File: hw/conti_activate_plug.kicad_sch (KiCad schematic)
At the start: 38 parts, among them J1 Conn_01x02_Pin, J2 Conn_01x02_Pin, J3 Conn_01x02_Pin, J4 Conn_01x02_Pin, J5 Conn_01x02_Pin, J6 Conn_01x02_Pin, J7 Conn_01x02_Socket, Q1 BSS138, Q2 MMBTA06, Q3 BSS138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

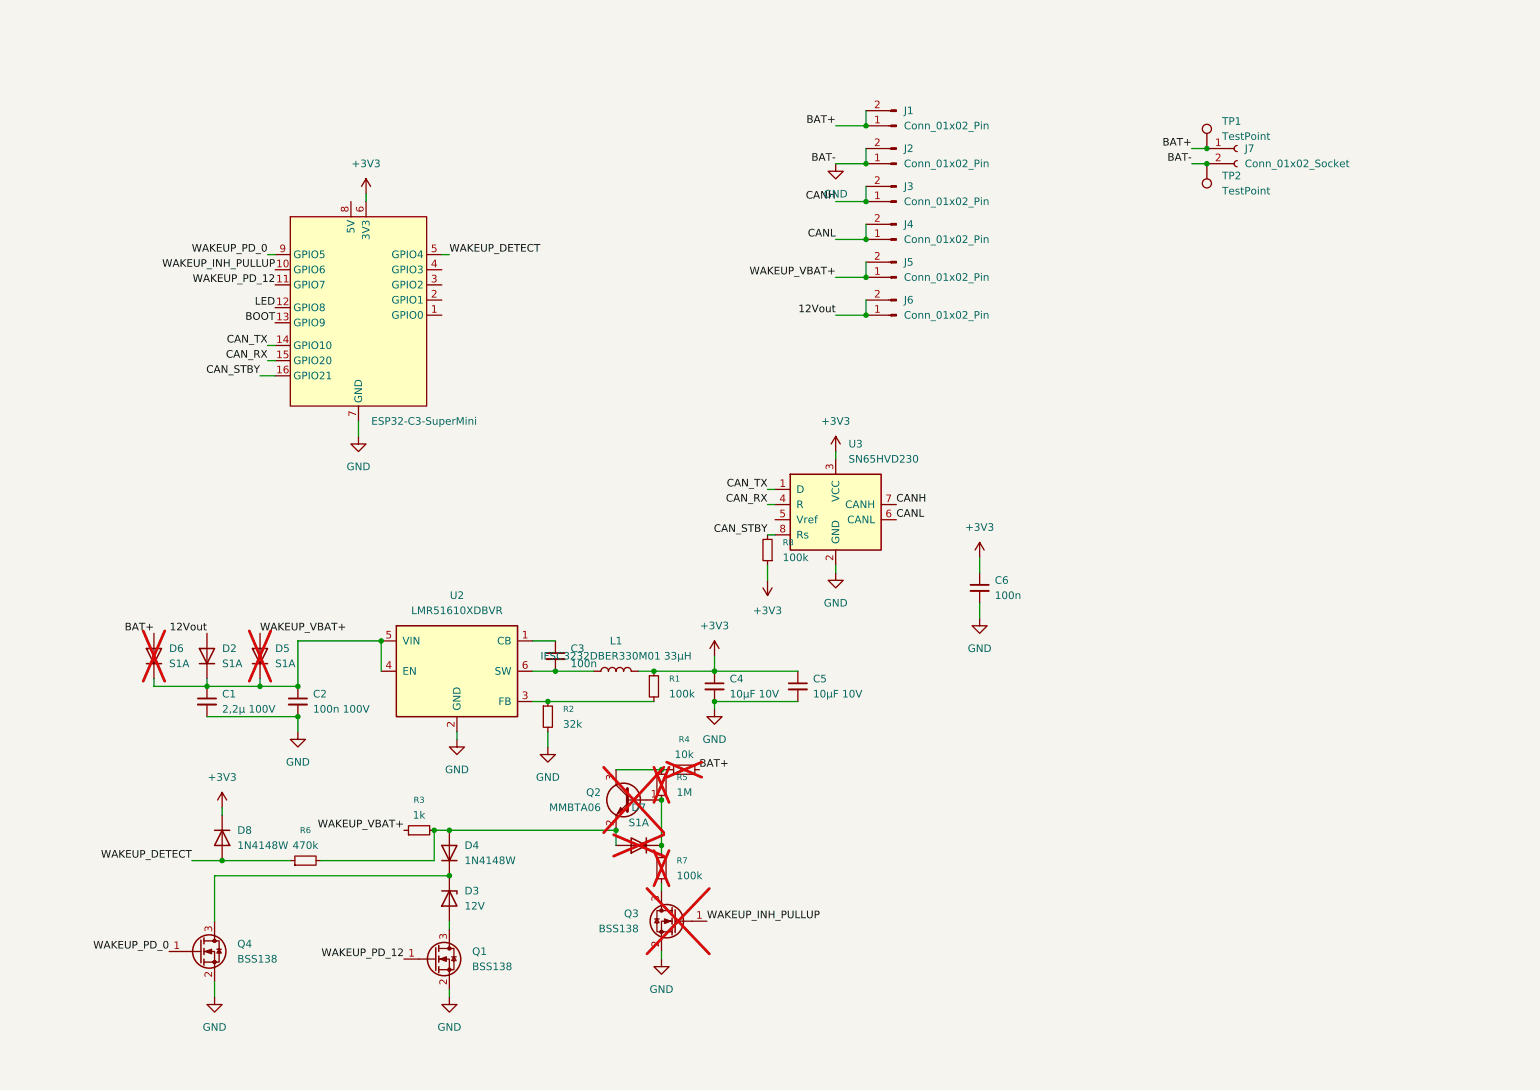
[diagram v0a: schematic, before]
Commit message: Vext, CAN Terminierung, Mounting-Hole
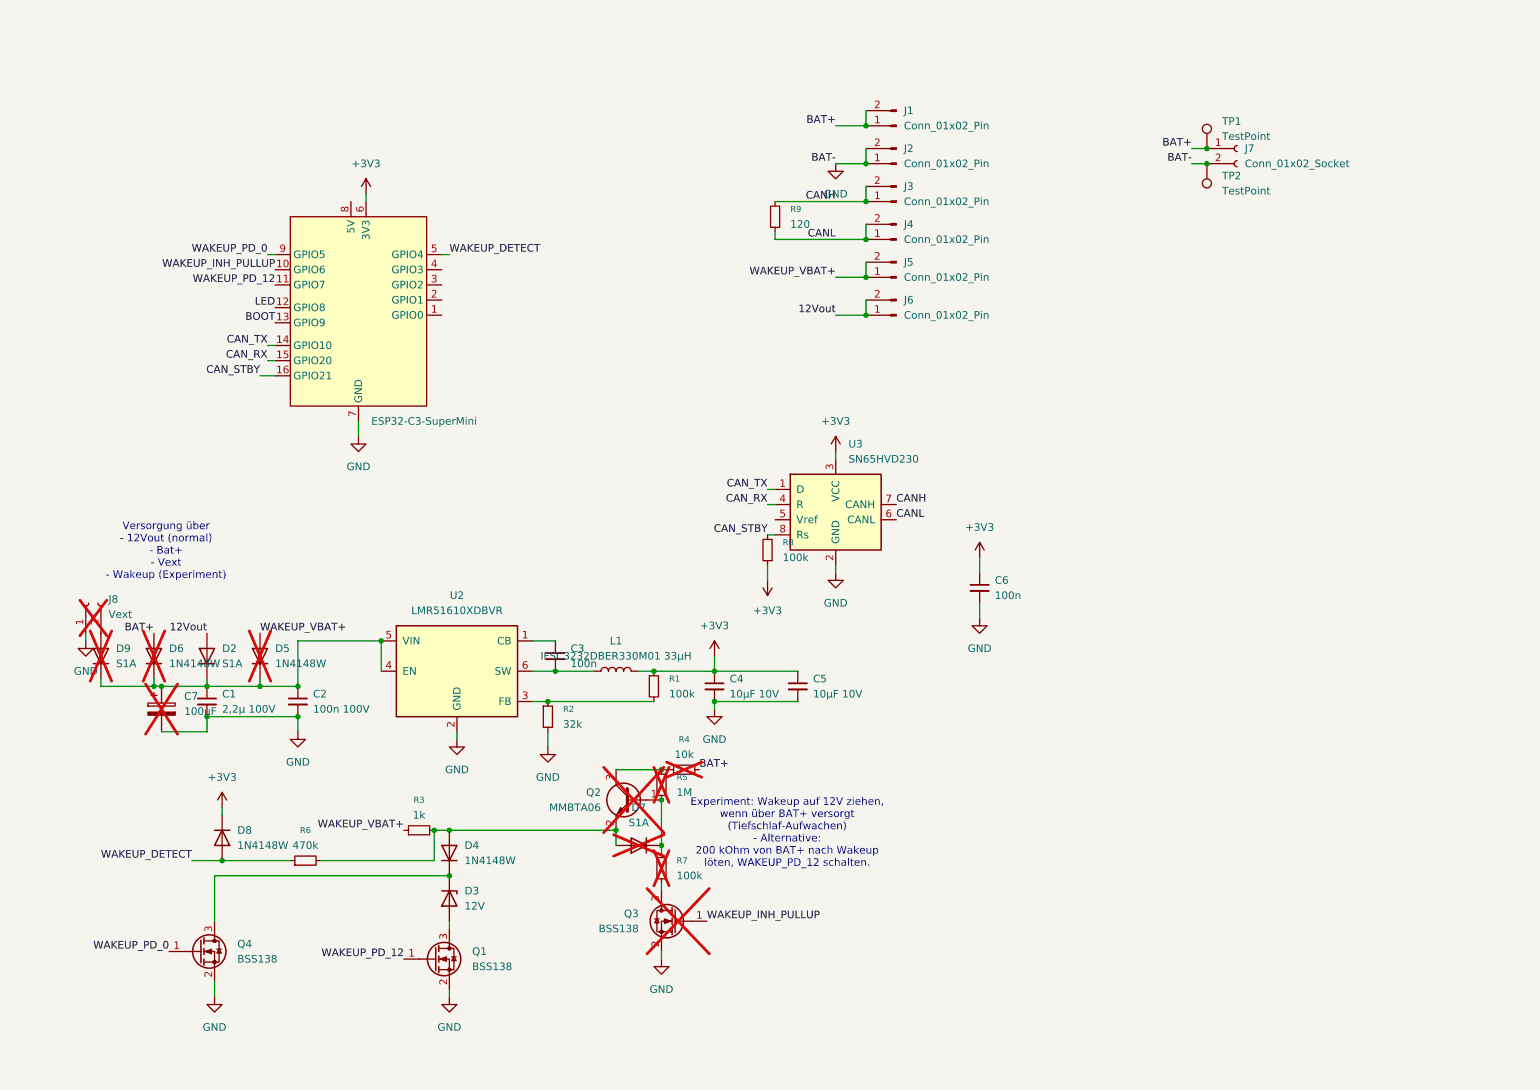
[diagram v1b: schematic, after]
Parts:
- added C7: 100µF, Capacitor_THT:CP_Radial_Tantal_D8.0mm_P5.00mm, symbol Device:C_Polarized
- added D9: S1A, Diode_SMD:D_SMA, symbol Diode:US1A
- added J8: Vext, Connector_PinHeader_2.54mm:PinHeader_1x02_P2.54mm_Vertical, symbol Connector:Conn_01x02_Socket
- added R9: 120, Resistor_SMD:R_0603_1608Metric, symbol Device:R_Small
- D5, D6: value S1A -> 1N4148W; footprint Diode_SMD:D_SMA -> Diode_SMD:D_SOD-123; symbol Diode:US1A -> Diode:1N4148W
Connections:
- net CANH: now also R9.2
- net CANL: now also R9.1
- net GND: now also C7.2, J8.1 (Pin_1)
- net at C1.1, C2.1, D2.1 (K)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: now also C7.1, D9.1 (K)
- new net: D9.2 (A), J8.2 (Pin_2)
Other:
- note added: "Experiment: Wakeup auf 12V ziehen, wenn über BAT+ versorgt (Tiefschlaf-Aufwachen) - Alternative: 200 kOhm von BAT+ nach Wakeup löten, WAKEUP_PD_12 schalten."
- note added: "Versorgung über - 12Vout (normal) - Bat+ - Vext - Wakeup (Experiment)"

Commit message: Stepdown redesigned, TCAN3414, S1B
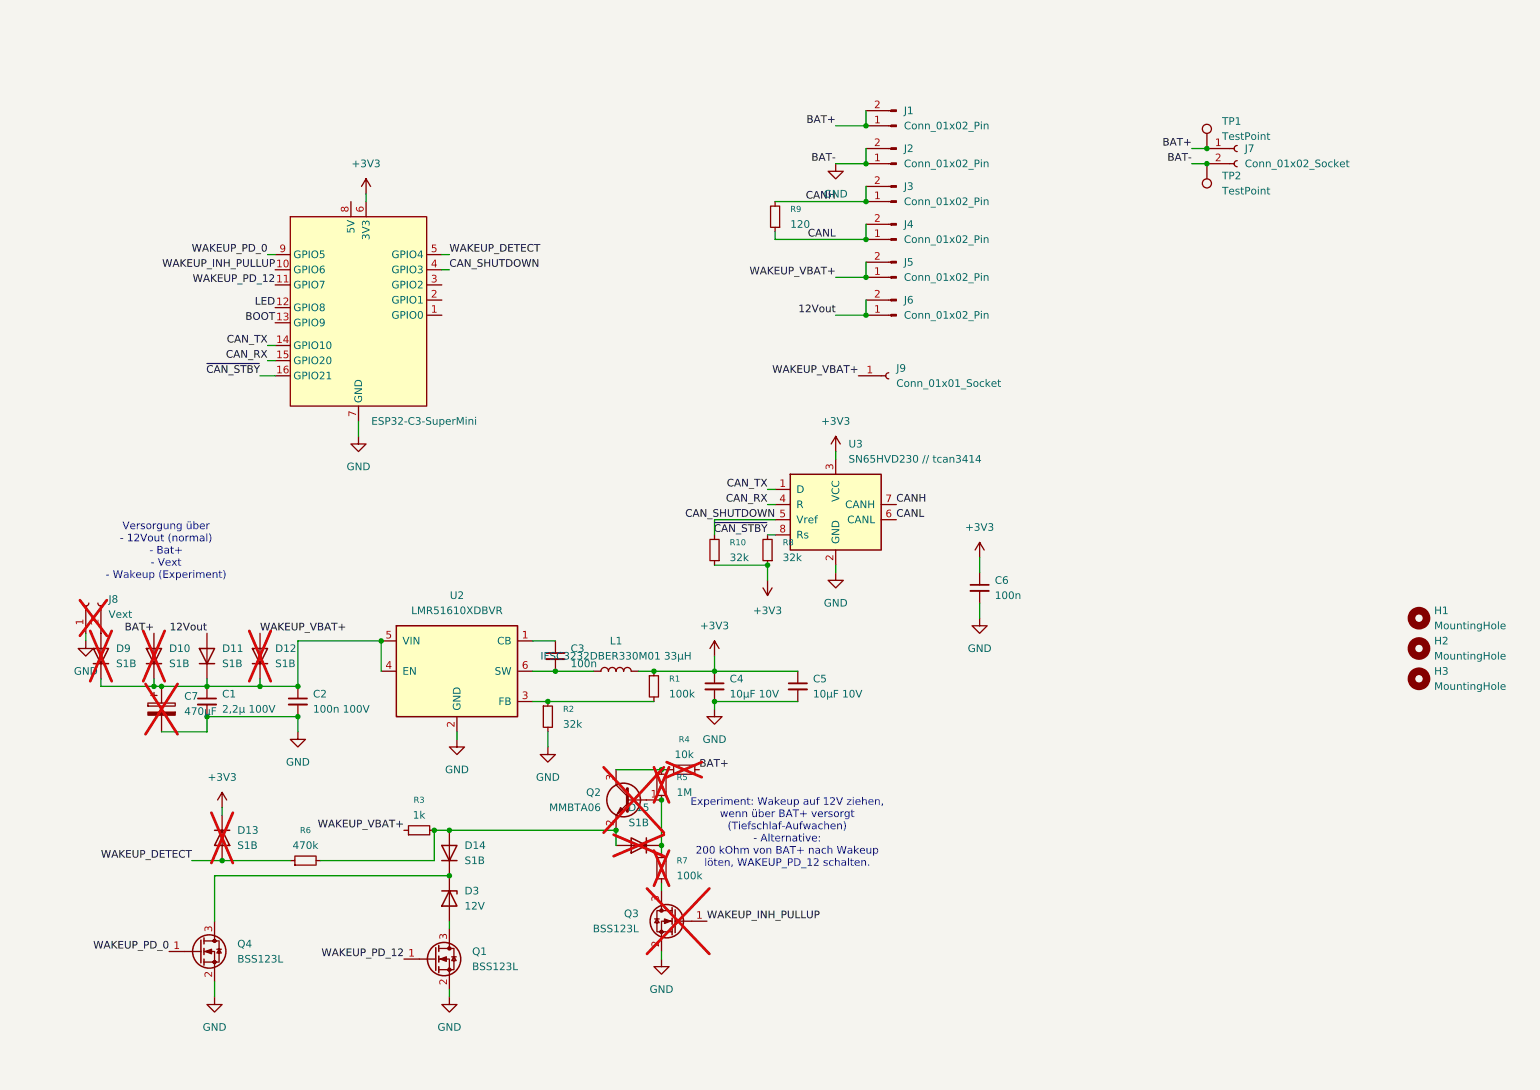
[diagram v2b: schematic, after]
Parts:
- removed D2, D7: S1A, Diode_SMD:D_SMA, symbol Diode:US1A
- removed D4, D5, D6, D8: 1N4148W, Diode_SMD:D_SOD-123, symbol Diode:1N4148W
- added D10, D11, D12, D13, D14, D15: S1B, Diode_SMD:D_SOD-123F, symbol Diode:US1A
- added H1, H2: MountingHole, MountingHole:MountingHole_3.2mm_M3, symbol Mechanical:MountingHole
- added H3: MountingHole, MountingHole:MountingHole_2.2mm_M2, symbol Mechanical:MountingHole
- added J9: Conn_01x01_Socket, Connector_PinHeader_2.54mm:PinHeader_1x01_P2.54mm_Vertical, symbol Connector:Conn_01x01_Socket
- added R10: 32k, Resistor_SMD:R_0603_1608Metric, symbol Device:R_Small
- C2: footprint Capacitor_SMD:C_0805_2012Metric -> Capacitor_SMD:C_0603_1608Metric
- C7: value 100µF -> 470µF
- D9: value S1A -> S1B; footprint Diode_SMD:D_SMA -> Diode_SMD:D_SOD-123F
- J1, J2, J3, J4, J5, J6: footprint TerminalBlock_MetzConnect:TerminalBlock_MetzConnect_Type073_RT02602HBLU_1x02_P5.08mm_Horizontal -> Library:1x02_P5.08mm
- Q1, Q3, Q4: value BSS138 -> BSS123L; symbol Transistor_FET:BSS138 -> Transistor_FET:BSS123
- R8: value 100k -> 32k
- U3: value SN65HVD230 -> SN65HVD230 // tcan3414
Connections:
- net +3V3: now also D13.1 (K), R10.1
- net 12Vout: now also D11.2 (A)
- net BAT+: now also D10.2 (A)
- net WAKEUP_DETECT: now also D13.2 (A)
- net WAKEUP_VBAT+: now also D12.2 (A), J9.1 (Pin_1)
- net at C1.1, C2.1, C7.1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: now also D10.1 (K), D11.1 (K), D12.1 (K)
- net at D3.1 (K), Q4.3 (D): now also D14.1 (K)
- net CAN_SHUTDOWN: now reaches U3.5 (Vref)
- net CAN_SHUTDOWN: now also U1.4 (GPIO3), R10.2
- net at Q2.1 (B), R5.2, R7.1: now also D15.1 (K)
- net at Q2.2 (E), R3.2, R6.2: now also D14.2 (A), D15.2 (A)
- net CAN_STBY renamed ~{CAN_STBY}

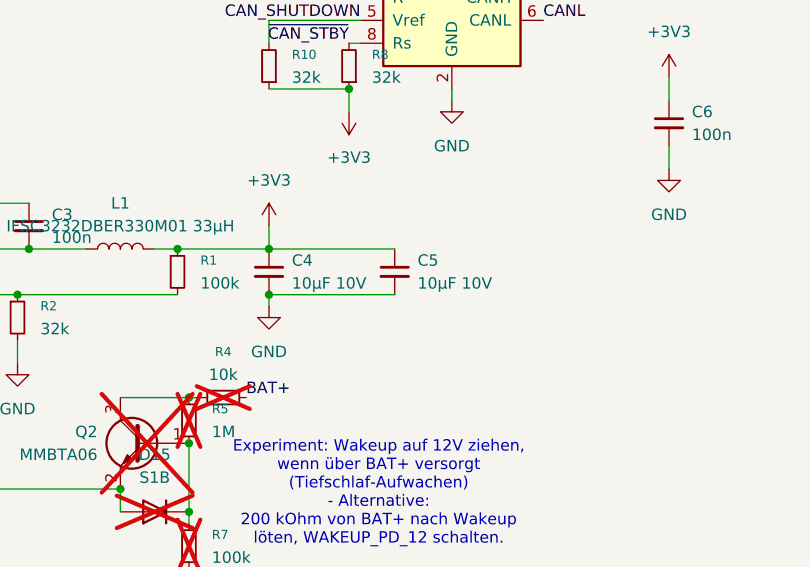
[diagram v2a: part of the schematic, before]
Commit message: paar Komponenten herausgesucht
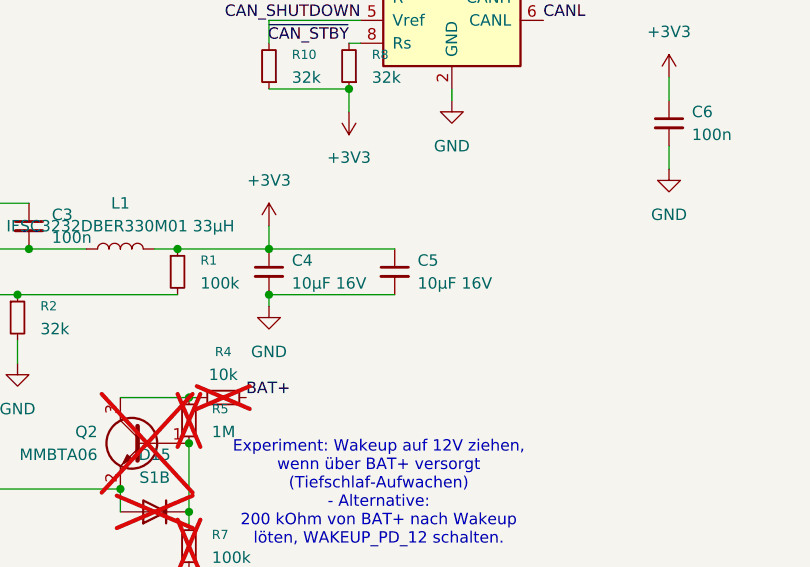
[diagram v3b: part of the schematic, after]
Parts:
- C1: Order (none) -> CL31B225KCHSNNE
- C4, C5: value 10µF 10V -> 10µF 16V; Order (none) -> CL21A106KOQNNNF
- D3: footprint Diode_SMD:D_SOD-323 -> Diode_SMD:D_SOD-123F
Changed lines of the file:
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@@
 			)
 		)
-		(property "Value" "10µF 10V"
+		(property "Value" "10µF 16V"
 			(at 134.62 129.5462 0)
 			(show_name no)
@@
 			)
 		)
+		(property "Order" "CL21A106KOQNNNF"
+			(at 132.08 128.27 0)
+			(hide yes)
+			(show_name no)
+			(do_not_autoplace no)
+			(effects
+				(font
+					(size 1.27 1.27)
+				)
+			)
+		)
 		(pin "1"
 		)
@@
 			)
 		)
-		(property "Footprint" "Diode_SMD:D_SOD-323"
+		(property "Footprint" "Diode_SMD:D_SOD-123F"
 			(at 87.63 163.83 0)
 			(hide yes)
@@
 			)
 		)
-		(property "Value" "10µF 10V"
+		(property "Value" "10µF 16V"
 			(at 148.59 129.5462 0)
 			(show_name no)
@@
 			)
 		)
+		(property "Order" "CL21A106KOQNNNF"
+			(at 146.05 128.27 0)
+			(hide yes)
+			(show_name no)
+			(do_not_autoplace no)
+			(effects
+				(font
+					(size 1.27 1.27)
+				)
+			)
+		)
 		(pin "1"
 		)
@@
 			(at 46.99 130.81 0)
 			(hide yes)
+			(show_name no)
+			(do_not_autoplace no)
+			(effects
+				(font
+					(size 1.27 1.27)
+				)
+			)
+		)
+		(property "Order" "CL31B225KCHSNNE"
+			(at 46.99 130.81 0)
+			(hide yes)

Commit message: forgot hw/sch
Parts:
- removed D14, D15: S1B, Diode_SMD:D_SOD-123F, symbol Diode:US1A
- removed Q2: MMBTA06, Package_TO_SOT_SMD:SOT-23, symbol Transistor_BJT:MMBTA06
- removed Q3: BSS123L, Package_TO_SOT_SMD:SOT-23, symbol Transistor_FET:BSS123
- removed R4: 10k, Resistor_SMD:R_0603_1608Metric, symbol Device:R_Small
- removed R5: 1M, Resistor_SMD:R_0603_1608Metric, symbol Device:R_Small
- removed R7: 100k, Resistor_SMD:R_0603_1608Metric, symbol Device:R_Small
- added C8: 100n 100V, Capacitor_SMD:C_0603_1608Metric, symbol Device:C_Small
- added JP1: Jumper_2_Bridged, Jumper:SolderJumper-2_P1.3mm_Bridged_RoundedPad1.0x1.5mm, symbol Jumper:Jumper_2_Bridged
- added JP2: Jumper_2_Open, Jumper:SolderJumper-2_P1.3mm_Open_RoundedPad1.0x1.5mm, symbol Jumper:Jumper_2_Open
- added Q2: BSS123L, Package_TO_SOT_SMD:SOT-23, symbol Transistor_FET:BSS123
- added Q3: BSS83P, Package_TO_SOT_SMD:SOT-23, symbol Transistor_FET:BSS83P
- added R11: 470k, Resistor_SMD:R_0603_1608Metric, symbol Device:R_Small
- added R12: 33k, Resistor_SMD:R_0603_1608Metric, symbol Device:R_Small
- added R13: 100k, Resistor_SMD:R_0603_1608Metric, symbol Device:R_Small
- added R14: 1M, Resistor_SMD:R_0603_1608Metric, symbol Device:R_Small
- added R15: 2R2, Resistor_SMD:R_0603_1608Metric, symbol Device:R_Small
- C1: LCSC (none) -> C13585
- C2, C3, C6: LCSC (none) -> C14663
- C4, C5: LCSC (none) -> C45783
- D10, D13, D9: LCSC (none) -> C64898; now fitted
- D11, D12: LCSC (none) -> C64898
- D3: LCSC (none) -> C22395569
- H3: footprint MountingHole:MountingHole_2.2mm_M2 -> MountingHole:MountingHole_3.2mm_M3
- J9: now not fitted
- L1: LCSC (none) -> C354641
- Q1, Q4: LCSC (none) -> C7420338
- R1: LCSC (none) -> C25803
- R10, R2, R8: value 32k -> 33k; LCSC (none) -> C4216
- R3: LCSC (none) -> C21190
- R6: value 470k -> 1M; LCSC (none) -> C22935
- R9: LCSC (none) -> C22787
- U2: LCSC (none) -> C20539658
- U3: LCSC (none) -> C12084
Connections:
- net +3V3: now also JP1.2 (B); no longer C4.1, C5.1, D13.1 (K), L1.2, R1.1
- net BAT+: now also D13.2 (A)
- net GND: now also C8.2, Q2.2 (S), R11.1, R12.1
- net WAKEUP_DETECT: now also C8.1, R12.2; no longer D13.2 (A)
- net at C1.1, C2.1, C7.1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: now also R15.1; no longer D10.1 (K), D11.1 (K), D12.1 (K), D9.1 (K)
- net at D3.1 (K), Q4.3 (D): now also R3.2, R6.2, Q3.3 (D), R11.2
- net at U1.8 (5V): now also JP2.2 (B)
- net WAKEUP_INH_PULLUP renamed WAKEUP_PU
- net WAKEUP_PU: now also Q2.1 (G)
- new net: D10.1 (K), D11.1 (K), D12.1 (K), D9.1 (K), R15.2
- new net: D13.1 (K), Q3.2 (S), R13.1
- new net: Q3.1 (G), R13.2, R14.1
- new net: Q2.3 (D), R14.2
- new net +5V: C4.1, C5.1, JP1.1 (A), JP2.1 (A), L1.2, R1.1
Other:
- note added: "Achtung: Standardkonfiguration: Stepdown auf 3,3V. Optionale Konfiguration: R2 20k für 5V, dann Lötbrücke 5V 3,3V trennen. Lötbrücke 5V in zum ESP schließen Dann Versorgung über LDO vom ESP."
- note added: "C7 bestücken, wenn der Akku Standalone neustarten können muss per Wakeup Trigger (Überbrückt ESP Versorgung für paar hundert ms)"
- note added: "Passiv: R3 brücken oder klein bestücken (0-1k) Q1 brücken von 2 nach 3 D3 bestücken ggf. Q4 von 2 nach 3 mit Kondensator (0805, 10µF) bestücken Für den Kondensator: R11 als Entladewiderstand mit >>100k Ohm bestücken"
- note removed: "Experiment: Wakeup auf 12V ziehen, wenn über BAT+ versorgt (Tiefschlaf-Aufwachen) - Alternative: 200 kOhm von BAT+ nach Wakeup löten, WAKEUP_PD_12 schalten."
- moved on the sheet: C1, C2, C7, D11, D12, J8

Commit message: v2
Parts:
- added R16, R19, R5, R7: 100k, Resistor_SMD:R_0603_1608Metric, symbol Device:R_Small
- added R17, R4: 33k, Resistor_SMD:R_0603_1608Metric, symbol Device:R_Small
- added R18: 1M, Resistor_SMD:R_0603_1608Metric, symbol Device:R_Small
- added R20: 470k, Resistor_SMD:R_0603_1608Metric, symbol Device:R_Small
- C4, C5: value 10µF 16V -> 22µF 25V; Order CL21A106KOQNNNF -> CL21A226MAQNNNE
- R11: LCSC (none) -> C23178
- R9: value 120 -> 200; LCSC C22787 -> C8218
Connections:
- net BAT+: now also R18.2
- net GND: now also R16.2, R17.2, R19.2, R5.2, R7.2
- net WAKEUP_PD_0: now also R16.1
- net WAKEUP_PD_12: now also R7.1
- net WAKEUP_PU: now also R5.1
- net at C1.1, C2.1, C7.1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: now also R20.1; no longer U2.4 (EN)
- net at D3.1 (K), Q4.3 (D), R11.2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: now also R4.1; no longer Q3.3 (D)
- net at U1.1 (GPIO0): now also R17.1, R18.1
- new net: R19.1, R20.2, U2.4 (EN)
- new net: Q3.3 (D), R4.2
